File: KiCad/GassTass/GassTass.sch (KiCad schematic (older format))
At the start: 19 parts, among them J1 EURO_PWR_2x5, U1 Arduino_Nano_v3.x, U2 ATmega328P-PU

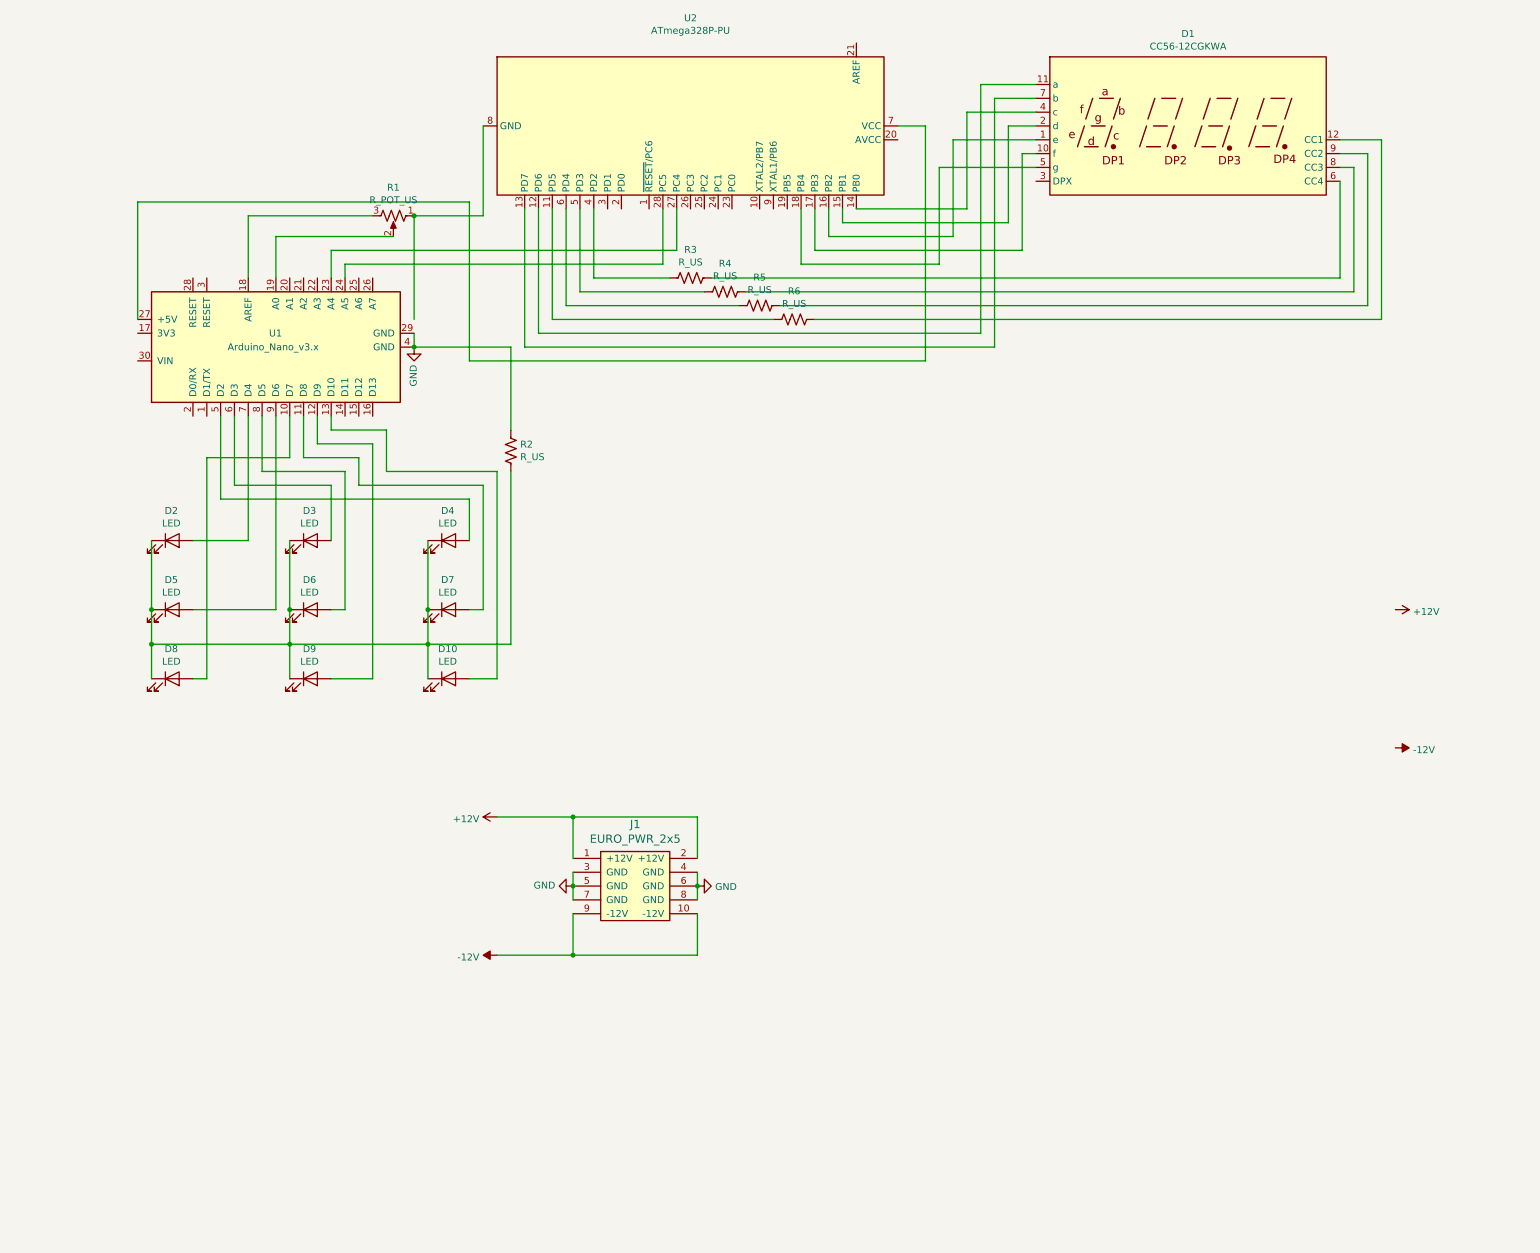
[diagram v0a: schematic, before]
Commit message: at it again, adding transistors
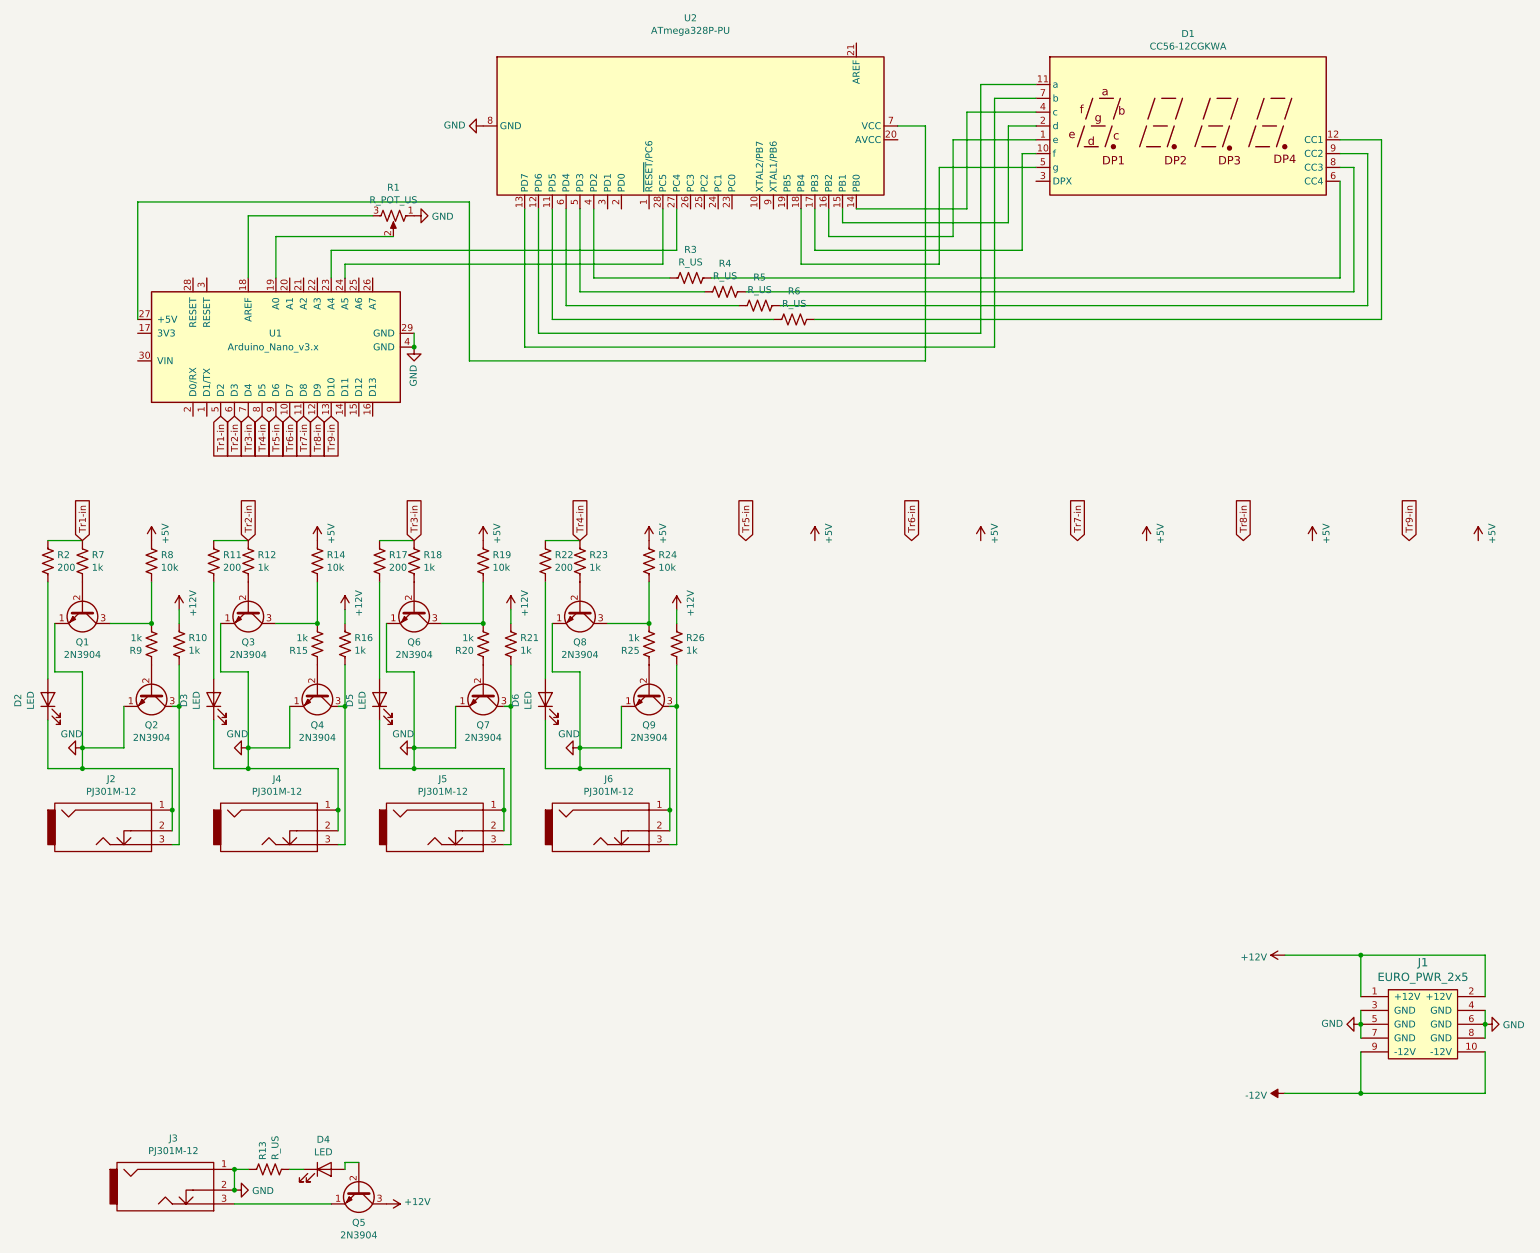
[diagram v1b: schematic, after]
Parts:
- removed D10, D7, D8, D9: LED, LED_THT:LED_D3.0mm_FlatTop, symbol Device:LED
- added J2, J3, J4, J5, J6: PJ301M-12, eurorack:PJ301M-12, symbol Eurorack:PJ301M-12
- added Q1, Q2, Q3, Q4, Q5, Q6, Q7, Q8, Q9: 2N3904, Package_TO_SOT_THT:TO-92_Inline, symbol Transistor_BJT:2N3904
- added R10, R12, R15, R16, R18, R20, R21, R23, R25, R26, R7, R9: 1k, Resistor_THT:R_Axial_DIN0207_L6.3mm_D2.5mm_P10.16mm_Horizontal, symbol Device:R_US
- added R11, R17, R22: 200, Resistor_THT:R_Axial_DIN0207_L6.3mm_D2.5mm_P10.16mm_Horizontal, symbol Device:R_US
- added R13: R_US, Resistor_THT:R_Axial_DIN0207_L6.3mm_D2.5mm_P10.16mm_Horizontal, symbol Device:R_US
- added R14, R19, R24, R8: 10k, Resistor_THT:R_Axial_DIN0207_L6.3mm_D2.5mm_P10.16mm_Horizontal, symbol Device:R_US
- R2: value R_US -> 200
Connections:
- net +12V: now also Q5.3 (C), R10.1, R16.1, R21.1, R26.1
- net GND: now also D2.1 (K), D3.1 (K), D5.1 (K), D6.1 (K), R1.1, U2.22 (GND), U2.8 (GND), J2.1, J2.2, J3.1, J3.2, J4.1, J4.2, J5.1, J5.2, J6.1, J6.2, Q1.1 (E), Q2.1 (E), Q3.1 (E), Q4.1 (E), Q6.1 (E), Q7.1 (E), Q8.1 (E), Q9.1 (E), R13.1; no longer R2.1
- net Tr6-in: now reaches U1.10 (D7)
- net Tr7-in: now reaches U1.11 (D8)
- net Tr8-in: now reaches U1.12 (D9)
- net Tr9-in: now reaches U1.13 (D10)
- net at D4.2 (A): now also Q5.2 (B); no longer U1.5 (D2)
- net at D3.2 (A): now also R11.2; no longer U1.6 (D3)
- net at D2.2 (A): now also R2.2; no longer U1.7 (D4)
- net at D6.2 (A): now also R22.2; no longer U1.8 (D5)
- net at D5.2 (A): now also R17.2; no longer U1.9 (D6)
- new net: J3.3, Q5.1 (E)
- new net: D4.1 (K), R13.2
- new net: Q1.3 (C), R8.2, R9.2
- new net: Q2.2 (B), R9.1
- new net: J2.3, Q2.3 (C), R10.2
- new net: Q1.2 (B), R7.2
- new net: Q3.3 (C), R14.2, R15.2
- new net: Q4.2 (B), R15.1
- new net: J4.3, Q4.3 (C), R16.2
- new net: Q3.2 (B), R12.2
- new net: Q6.3 (C), R19.2, R20.2
- new net: Q7.2 (B), R20.1
- new net: J5.3, Q7.3 (C), R21.2
- new net: Q6.2 (B), R18.2
- new net: Q8.3 (C), R24.2, R25.2
- new net: Q9.2 (B), R25.1
- new net: J6.3, Q9.3 (C), R26.2
- new net: Q8.2 (B), R23.2
- new net +5V: R14.1, R19.1, R24.1, R8.1
- new net Tr1-in: R2.1, R7.1, U1.5 (D2)
- new net Tr2-in: R11.1, R12.1, U1.6 (D3)
- new net Tr3-in: R17.1, R18.1, U1.7 (D4)
- new net Tr4-in: R22.1, R23.1, U1.8 (D5)
- new net Tr5-in: U1.9 (D6)
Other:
- moved on the sheet: J1
